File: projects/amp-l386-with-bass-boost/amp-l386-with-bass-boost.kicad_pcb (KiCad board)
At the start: 2 copper layers, 102.4 x 75.2 mm, 12 parts, among them J1 AudioJack, J2 Jack-DC, U1 LM386

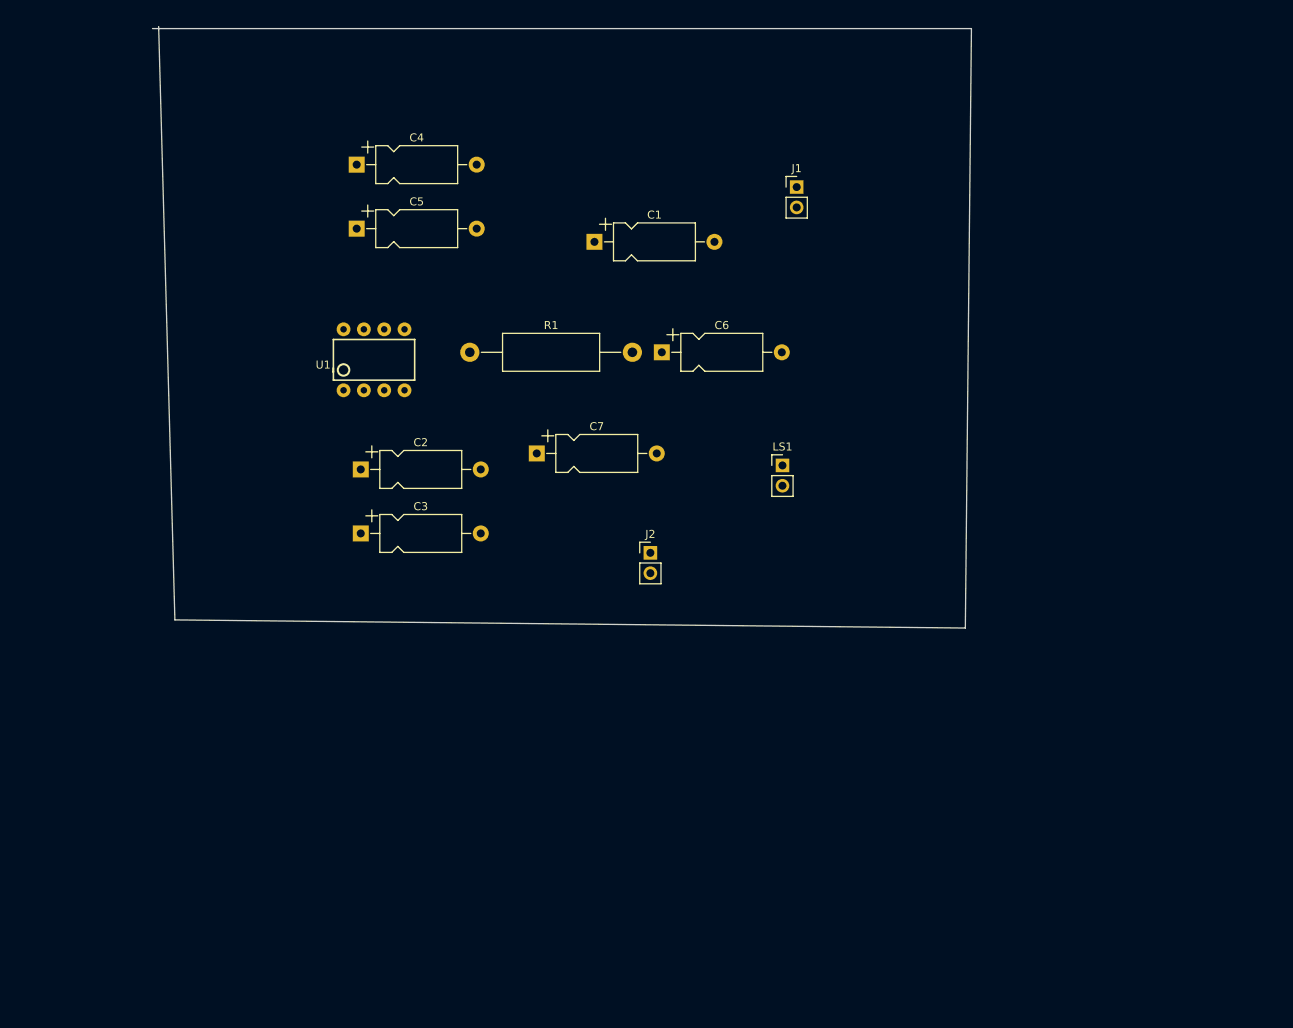
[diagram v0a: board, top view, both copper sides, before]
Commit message: Checking initial PCB placement of bassboost project
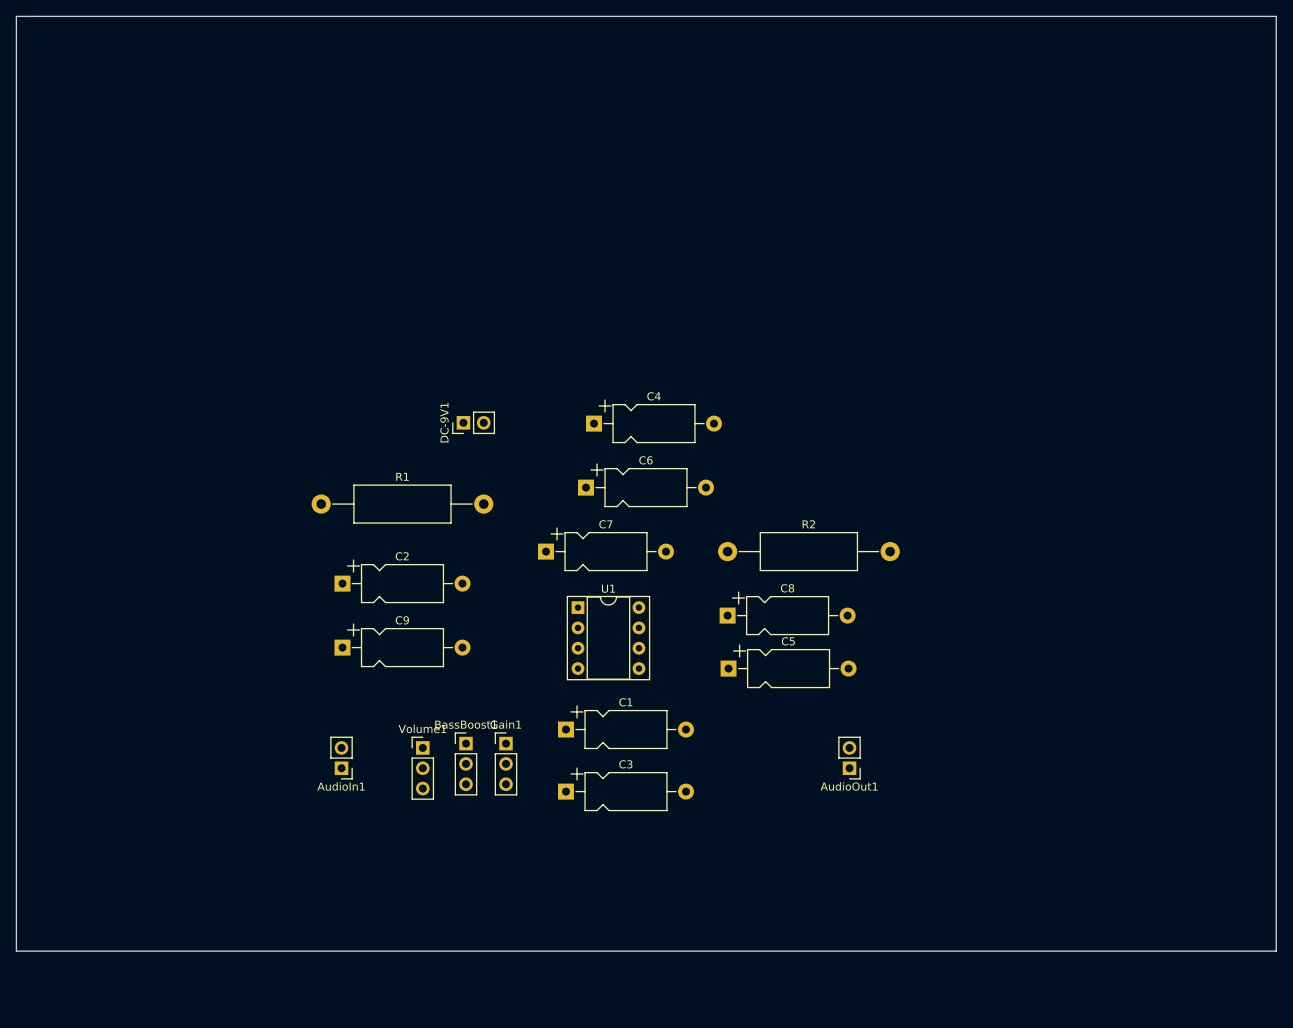
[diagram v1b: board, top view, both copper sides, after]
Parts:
- removed J1: AudioJack, jme:jme-audio-pinheader-2.54-vertical
- removed J2: Jack-DC, Connector_PinHeader_2.54mm:PinHeader_1x02_P2.54mm_Vertical
- removed LS1: Speaker, Connector_PinHeader_2.54mm:PinHeader_1x02_P2.54mm_Vertical
- added AudioIn1: AudioJack, jme:jme-audio-pinheader-2.54-vertical, F.Cu at (91.4, 132.1)
- added AudioOut1: Speaker, Connector_PinHeader_2.54mm:PinHeader_1x02_P2.54mm_Vertical, F.Cu at (154.9, 132.1)
- added BassBoost1: 10K, Connector_PinHeader_2.54mm:PinHeader_1x03_P2.54mm_Vertical, F.Cu at (107.0, 129.0)
- added C8: 10uF, Capacitor_THT:CP_Axial_L10.0mm_D4.5mm_P15.00mm_Horizontal, F.Cu at (139.7, 113.0)
- added C9: 0.033uF, Capacitor_THT:CP_Axial_L10.0mm_D4.5mm_P15.00mm_Horizontal, F.Cu at (91.6, 117.0)
- added DC-9V1: Jack-DC, Connector_PinHeader_2.54mm:PinHeader_1x02_P2.54mm_Vertical, F.Cu at (106.7, 88.9)
- added Gain1: 10K, Connector_PinHeader_2.54mm:PinHeader_1x03_P2.54mm_Vertical, F.Cu at (112.0, 129.0)
- added R2: 10K, Resistor_THT:R_Axial_DIN0414_L11.9mm_D4.5mm_P20.32mm_Horizontal, F.Cu at (139.7, 105.0)
- added Volume1: 10K, Connector_PinHeader_2.54mm:PinHeader_1x03_P2.54mm_Vertical, F.Cu at (101.6, 129.5)
- C1: value .27uF -> 1000uF
- C2: value 47pF -> 0.1uF
- C3: value .27uF -> 10uF
- C4: value .27uF -> 100uF
- C5: value 10uF -> 0.1uF
- C6: value .1uF -> 470pF
- C7: value 470uF -> 0.1uF
- R1: value 10 -> 10R
- U1: footprint LM386:DIP08 -> Package_DIP:DIP-8_W7.62mm_Socket
- moved C5 72.0 mm to (139.8, 119.6)
- moved C1 61.1 mm to (119.5, 127.2)
- moved C4 43.9 mm to (123.0, 89.0)
- moved C3 41.2 mm to (119.5, 135.0)
- moved U1 40.1 mm to (121.0, 112.0)
- moved R1 26.6 mm to (88.9, 99.1)
- moved C6 19.4 mm to (122.0, 97.0)
- moved C2 14.5 mm to (91.6, 109.0)
- moved C7 12.3 mm to (117.0, 105.0)
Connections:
- C1 pad 1: Net-(C1-Pad1) -> Net-(BassBoost1-Pad2)
- C2 pad 1: Net-(C1-Pad1) -> Net-(BassBoost1-Pad2)
- C2 pad 2: GND -> Net-(C2-Pad2)
- C3 pad 2: GND -> Net-(C3-Pad2)
- C5 pad 1: Net-(C5-Pad1) -> +9V
- C6 pad 1: Net-(C6-Pad1) -> GND
- C7 pad 1: Net-(C7-Pad1) -> +9V
- C7 pad 2: Net-(C7-Pad2) -> GND
- R1 pad 1: Net-(C7-Pad1) -> Net-(C2-Pad2)
- R1 pad 2: Net-(C6-Pad1) -> GND
- U1 pad 1: unconnected-(U1-Pad1) -> Net-(BassBoost1-Pad1)
- U1 pad 2: Net-(C3-Pad1) -> GND
- U1 pad 3: Net-(C1-Pad1) -> Net-(U1-Pad3)
- U1 pad 5: Net-(C7-Pad1) -> Net-(BassBoost1-Pad2)
- U1 pad 7: Net-(C5-Pad1) -> Net-(R2-Pad1)
- U1 pad 8: unconnected-(U1-Pad8) -> Net-(C3-Pad2)
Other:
- board size 102.4 x 75.2 mm -> 157.5 x 116.8 mm

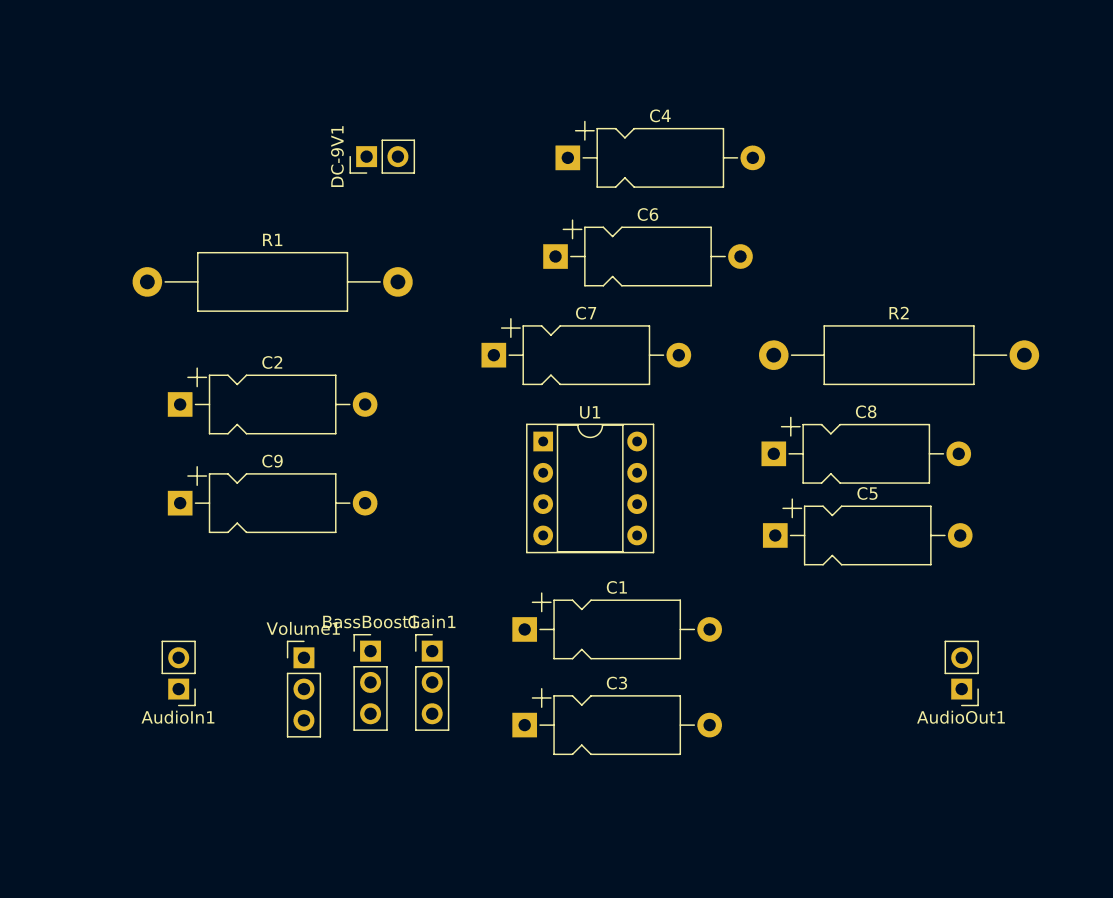
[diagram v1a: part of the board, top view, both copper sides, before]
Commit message: Progress on amp-l386-with-bass-boost layout. Still need real footprints
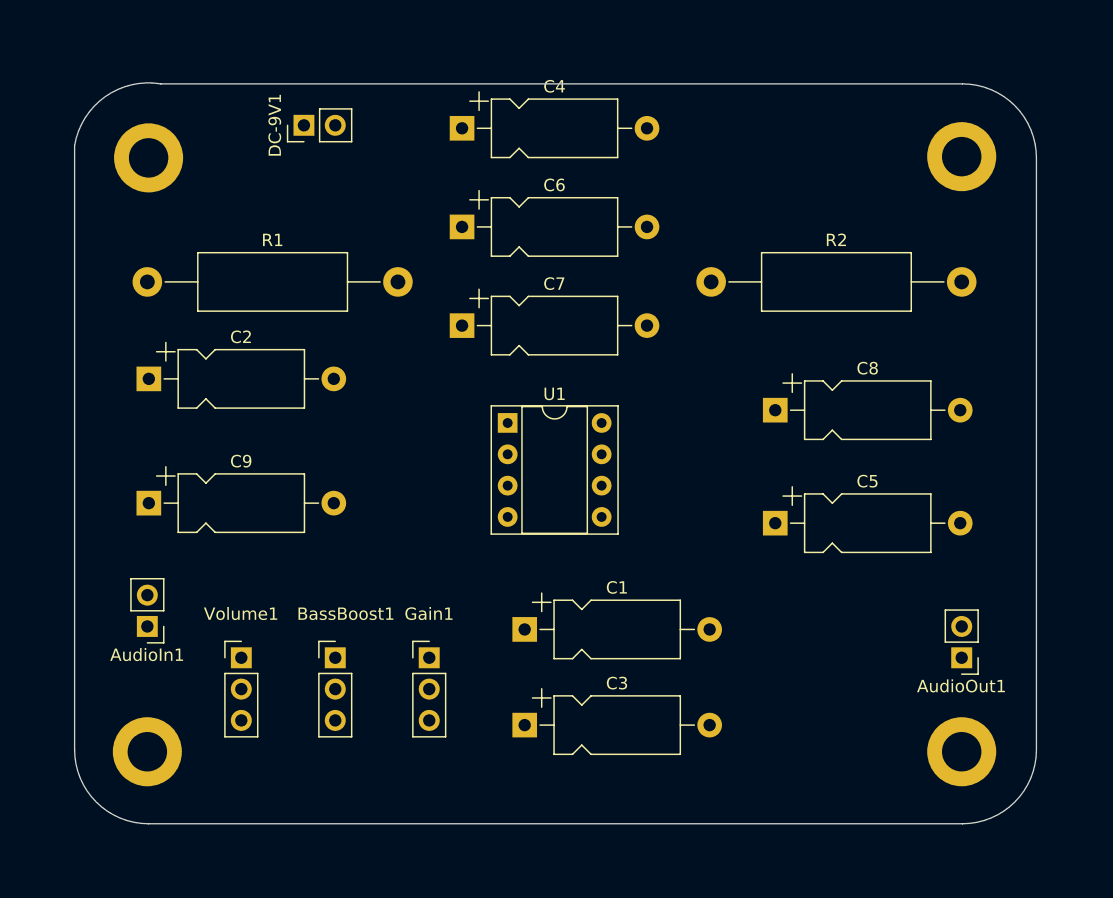
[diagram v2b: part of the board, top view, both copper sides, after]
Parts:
- added H1: MountingHole_Pad, MountingHole:MountingHole_3.2mm_M3_DIN965_Pad, F.Cu at (88.9, 137.2)
- added H2: MountingHole_Pad, MountingHole:MountingHole_3.2mm_M3_DIN965_Pad, F.Cu at (154.9, 137.2)
- added H3: MountingHole_Pad, MountingHole:MountingHole_3.2mm_M3_DIN965_Pad, F.Cu at (154.9, 88.9)
- added H4: MountingHole_Pad, MountingHole:MountingHole_3.2mm_M3_DIN965_Pad, F.Cu at (89.0, 89.0)
- moved C4 8.91 mm to (114.4, 86.6)
- moved C6 7.95 mm to (114.4, 94.6)
- moved R2 7.82 mm to (134.6, 99.1)
- moved DC-9V1 5.68 mm to (101.6, 86.4)
- moved AudioIn1 5.68 mm to (88.9, 127.0)
- moved Volume1 5.08 mm to (96.5, 129.5)
- moved C8 3.54 mm to (139.8, 109.5)
- moved C7 3.52 mm to (114.4, 102.6)
- moved C2 3.28 mm to (89.0, 106.9)
- moved U1 3.25 mm to (118.1, 110.5)
- moved BassBoost1 2.91 mm to (104.1, 129.5)
- moved AudioOut1 2.54 mm to (154.9, 129.5)
- moved C9 2.54 mm to (89.0, 117.0)
- moved C5 1.00 mm to (139.8, 118.6)
- moved Gain1 0.59 mm to (111.8, 129.5)
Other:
- outline, holes or cut-outs redrawn

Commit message: Add copper ground plane to PCB
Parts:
- moved C9 15.0 mm to (104.0, 116.6), turned to 180 degrees
- moved AudioOut1 7.62 mm to (147.3, 129.5)
- moved C5 2.54 mm to (142.4, 118.6)
- moved C8 2.54 mm to (142.4, 109.5)
- moved R2 2.54 mm to (137.2, 99.1)
- turned DC-9V1 to 0 degrees
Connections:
- C1 pad 1: Net-(BassBoost1-Pad2) -> Net-(C1-Pad1)
- C2 pad 1: Net-(BassBoost1-Pad2) -> Net-(C1-Pad1)
- C9 pad 1: Net-(BassBoost1-Pad2) -> Net-(C1-Pad1)
- U1 pad 5: Net-(BassBoost1-Pad2) -> Net-(C1-Pad1)
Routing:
- net +9V: track 0.00 -> 63.4 mm
- net Net-(C1-Pad1): track 0.00 -> 30.9 mm
- net Net-(U1-Pad3): track 0.00 -> 28.4 mm
- net Net-(C8-Pad1): track 0.00 -> 19.4 mm
- net Net-(R2-Pad1): track 0.00 -> 18.7 mm
- net Net-(C2-Pad2): track 0.00 -> 18.4 mm
- net Net-(AudioOut1-Pad1): track 0.00 -> 13.8 mm
- net Net-(AudioIn1-PadT): track 0.00 -> 9.72 mm
- net Net-(BassBoost1-Pad1): track 0.00 -> 8.67 mm
- net Net-(C3-Pad1): track 0.00 -> 7.90 mm
- added copper zone on B.Cu, net GND
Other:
- board size 157.5 x 116.8 mm -> 78 x 60.1 mm

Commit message: Incremental changes optimizing PCB layout
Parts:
- C6: value 470pF -> 470pF w/2&4
- moved R1 60.6 mm to (135.3, 138.0)
- moved DC-9V1 59.2 mm to (158.5, 102.7)
- moved AudioOut1 52.5 mm to (95.5, 138.0)
- moved C2 40.3 mm to (126.0, 123.0), turned to -90 degrees
- moved C3 40.1 mm to (99.5, 100.2)
- moved Gain1 38.6 mm to (87.0, 100.0), turned to 90 degrees
- moved C4 32.0 mm to (138.0, 108.2)
- moved C7 31.3 mm to (138.0, 123.2)
- moved BassBoost1 28.3 mm to (87.0, 107.0)
- moved C6 22.9 mm to (95.5, 107.5), turned to -90 degrees
- moved Volume1 22.8 mm to (111.0, 112.0)
- moved H1 20.0 mm to (74.5, 151.0)
- moved C9 19.9 mm to (117.5, 131.3)
- moved AudioIn1 19.1 mm to (104.5, 116.0)
- moved H4 18.8 mm to (75.0, 76.5)
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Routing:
- net GND: track 0.00 -> 49.8 mm
- net Net-(C1-Pad1): track 30.9 -> 0.00 mm
- net Net-(U1-Pad3): track 28.4 -> 7.56 mm
- net Net-(C8-Pad1): track 19.4 -> 0.00 mm
- net Net-(R2-Pad1): track 18.7 -> 0.00 mm
- net Net-(C2-Pad2): track 18.4 -> 0.00 mm
- net +9V: track 63.4 -> 49.2 mm
- net Net-(AudioOut1-Pad1): track 13.8 -> 0.00 mm
- net Net-(BassBoost1-Pad1): track 8.67 -> 0.00 mm
- net Net-(C3-Pad1): track 7.90 -> 0.00 mm
- net Net-(AudioIn1-PadT): track 9.72 -> 7.12 mm
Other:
- board size 78 x 60.1 mm -> 135.5 x 102.5 mm

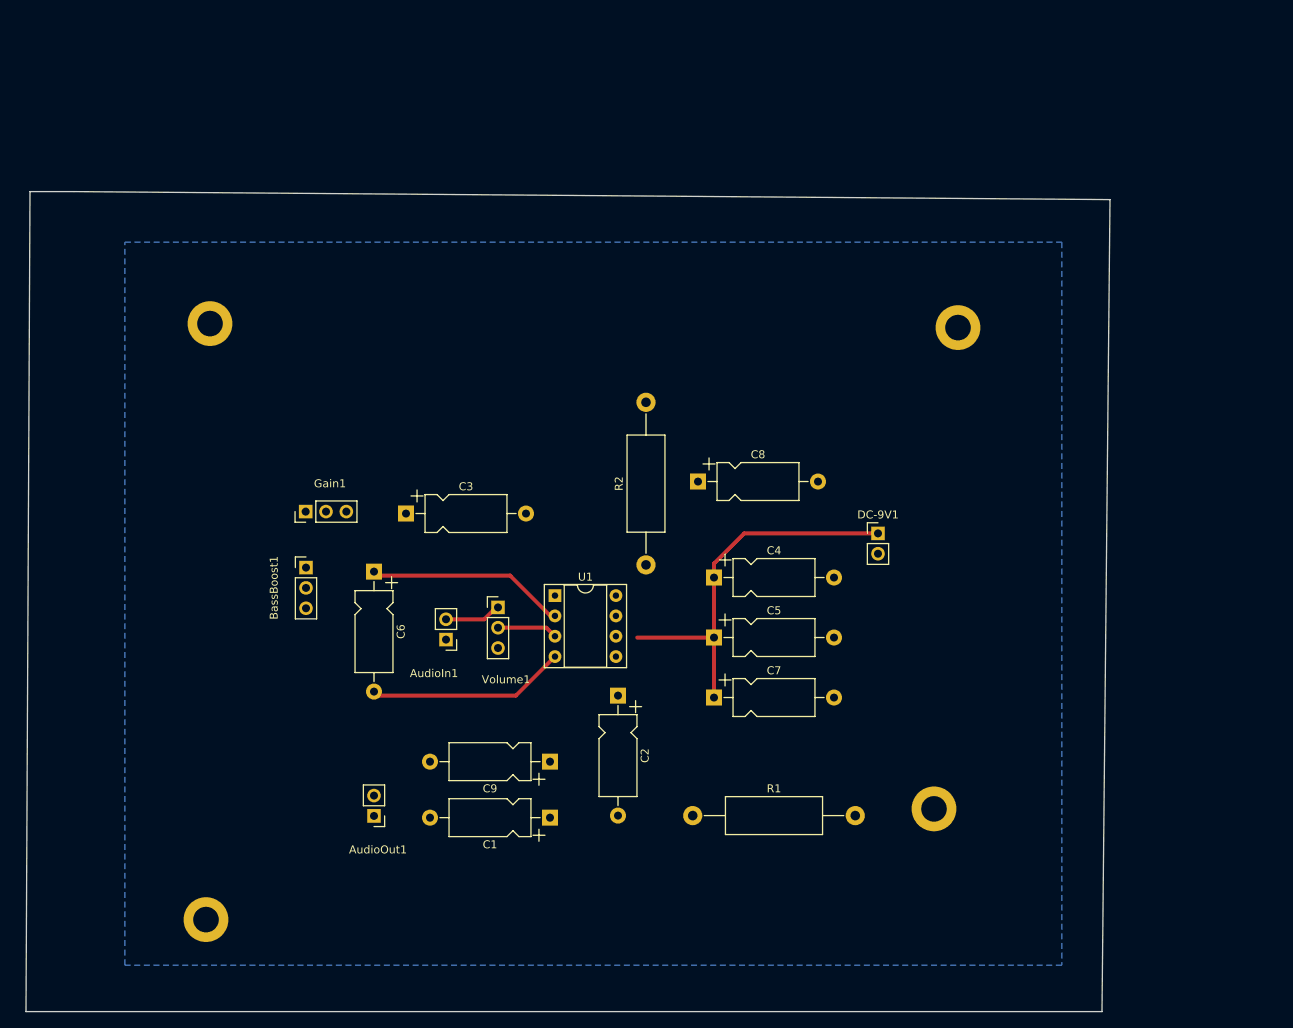
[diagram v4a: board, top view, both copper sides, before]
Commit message: Cleaned up with cut layer. Possibly complete. Time to validate.
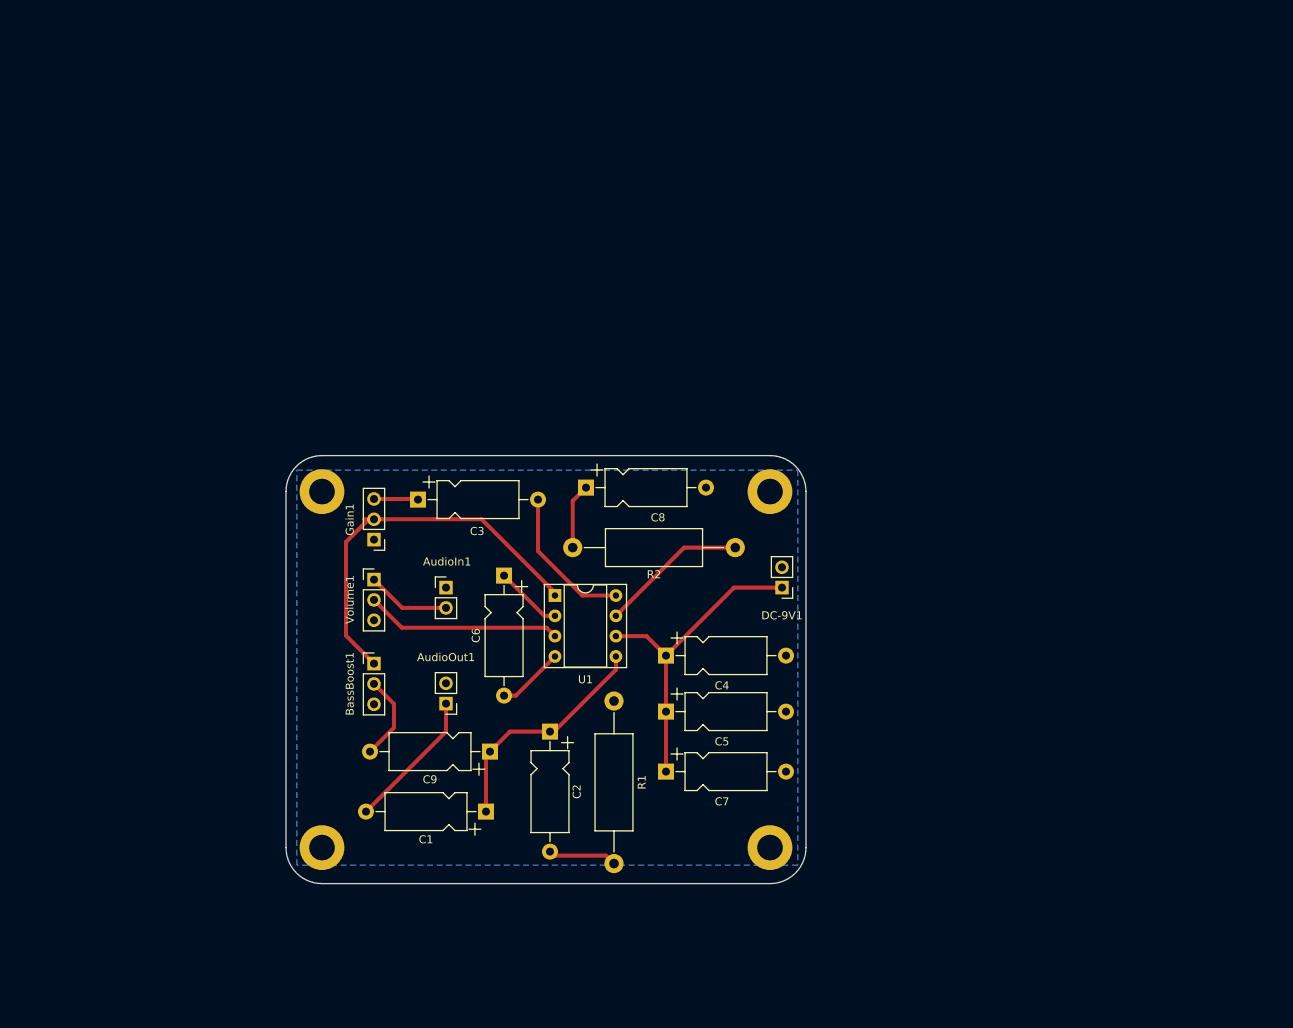
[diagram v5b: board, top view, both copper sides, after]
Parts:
- moved H3 31.2 mm to (145.0, 97.5)
- moved H4 25.2 mm to (89.0, 97.5)
- moved H2 21.1 mm to (145.0, 142.0)
- moved H1 17.1 mm to (89.0, 142.0)
- moved AudioOut1 16.7 mm to (104.5, 124.0)
- moved C6 16.3 mm to (111.8, 108.0)
- moved Volume1 15.9 mm to (95.5, 108.5)
- moved BassBoost1 14.7 mm to (95.5, 119.0)
- moved C8 14.0 mm to (122.0, 97.0)
- moved DC-9V1 13.8 mm to (146.5, 109.5), turned to 180 degrees
- moved R1 11.5 mm to (125.5, 144.0), turned to 90 degrees
- moved C4 11.5 mm to (132.0, 118.0)
- moved R2 11.4 mm to (140.7, 104.5), turned to 180 degrees
- moved C5 11.0 mm to (132.0, 125.0)
- moved C7 11.0 mm to (132.0, 132.5)
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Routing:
- net Net-(BassBoost1-Pad1): track 0.00 -> 49.3 mm
- net GND: track 49.8 -> 16.8 mm
- net Net-(C1-Pad1): track 0.00 -> 29.4 mm
- net Net-(C3-Pad2): track 0.00 -> 18.5 mm
- net Net-(R2-Pad1): track 0.00 -> 18.5 mm
- net Net-(AudioOut1-Pad1): track 0.00 -> 17.6 mm
- net Net-(U1-Pad3): track 7.56 -> 24.5 mm
- net Net-(BassBoost1-Pad2): track 0.00 -> 10.7 mm
- net +9V: track 49.2 -> 39.8 mm
- net Net-(C2-Pad2): track 0.00 -> 8.62 mm
- net Net-(C8-Pad1): track 0.00 -> 8.19 mm
- net Net-(C3-Pad1): track 0.00 -> 5.53 mm
- net Net-(AudioIn1-PadT): track 7.12 -> 10.5 mm
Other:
- board size 135.5 x 102.5 mm -> 65 x 53.5 mm
